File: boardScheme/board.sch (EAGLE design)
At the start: 24 parts, among them IC1 MEGA32-P, Q1 BC547, Q10 BC547, Q11 BC547, Q12 BC547, Q13 BC547, Q14 BC547, Q2 BC547, Q3 BC547, Q4 BC547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

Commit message: Changed board scheme.
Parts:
- added R1, R10, R11, R12, R13, R14, R2, R3, R4, R5, R6, R7, R8, R9: 10K, eagle-ltspice:R0204/7
- added R15, R16: 80R, eagle-ltspice:R0204/7
- added R17, R18, R19, R20, R21, R22, R23, R24: (no value), eagle-ltspice:R0204/7
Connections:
- new net N$23: Q2.B
- new net N$25: Q1.B, R1.2
- new net N$30: IC1.(AIN0/INT2)PB2, R3.1
- new net N$31: IC1.(AIN1/OC0)PB3, R4.1
- new net N$32: IC1.(SS)PB4, R5.1
- new net N$33: IC1.(MOSI)PB5, R6.1
- new net N$49: IC1.(MISO)PB6, R7.1
- new net N$50: IC1.(SCK)PB7, R8.1
- new net N$51: Q14.B, R9.2
- new net N$53: Q9.B, R11.2
- new net N$54: Q11.B, R13.2
- new net N$55: Q10.B, R12.2
- new net N$56: Q12.B, R14.2
- new net N$57: LED4.A, R15.2
- new net N$58: LED5.A, R16.2
- new net N$59: Q1.E, R17.2
- new net N$60: Q2.E, R18.2
- new net N$61: Q3.E, R19.2
- new net N$62: Q4.E, R20.2
- new net N$63: Q5.E, R21.2
- new net N$64: Q6.E, R22.2
- new net N$65: Q7.E, R23.2
- new net N$66: Q8.E, R24.2
- net N$11: now also R1.1; no longer Q1.B
- net N$13: now also R2.2
- net N$14: now also R2.1; no longer Q2.B
- net N$15: now also R3.2; no longer IC1.(AIN0/INT2)PB2
- net N$16: now also R4.2; no longer IC1.(AIN1/OC0)PB3
- net N$17: now also R5.2; no longer IC1.(SS)PB4
- net N$18: now also R6.2; no longer IC1.(MOSI)PB5
- net N$19: now also R7.2; no longer IC1.(MISO)PB6
- net N$20: now also R8.2; no longer IC1.(SCK)PB7
- net N$21: now also R17.1; no longer Q1.E
- net N$22: now also R20.1; no longer Q4.E
- net N$24: now also R18.1; no longer Q2.E
- net N$26: now also R19.1; no longer Q3.E
- net N$27: now also R23.1; no longer Q7.E
- net N$28: now also R21.1; no longer Q5.E
- net N$29: now also R11.1; no longer Q9.B
- net N$3: now also Q13.B, R10.2; no longer IC1.(OC1B)PD4, Q14.B
- net N$34: now also R12.1; no longer Q10.B
- net N$35: now also R24.1; no longer Q8.E
- net N$40: now also R13.1; no longer Q11.B
- net N$41: now also R14.1; no longer Q12.B
- net N$42: now also IC1.(OC2)PD7, R10.1, R9.1; no longer IC1.(OC1A)PD5, Q13.B
- net N$43: now also R15.1; no longer LED4.A
- net N$45: now also R16.1; no longer LED5.A
- net N$48: now also R22.1; no longer Q6.E
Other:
- moved on the sheet: LED4, LED5

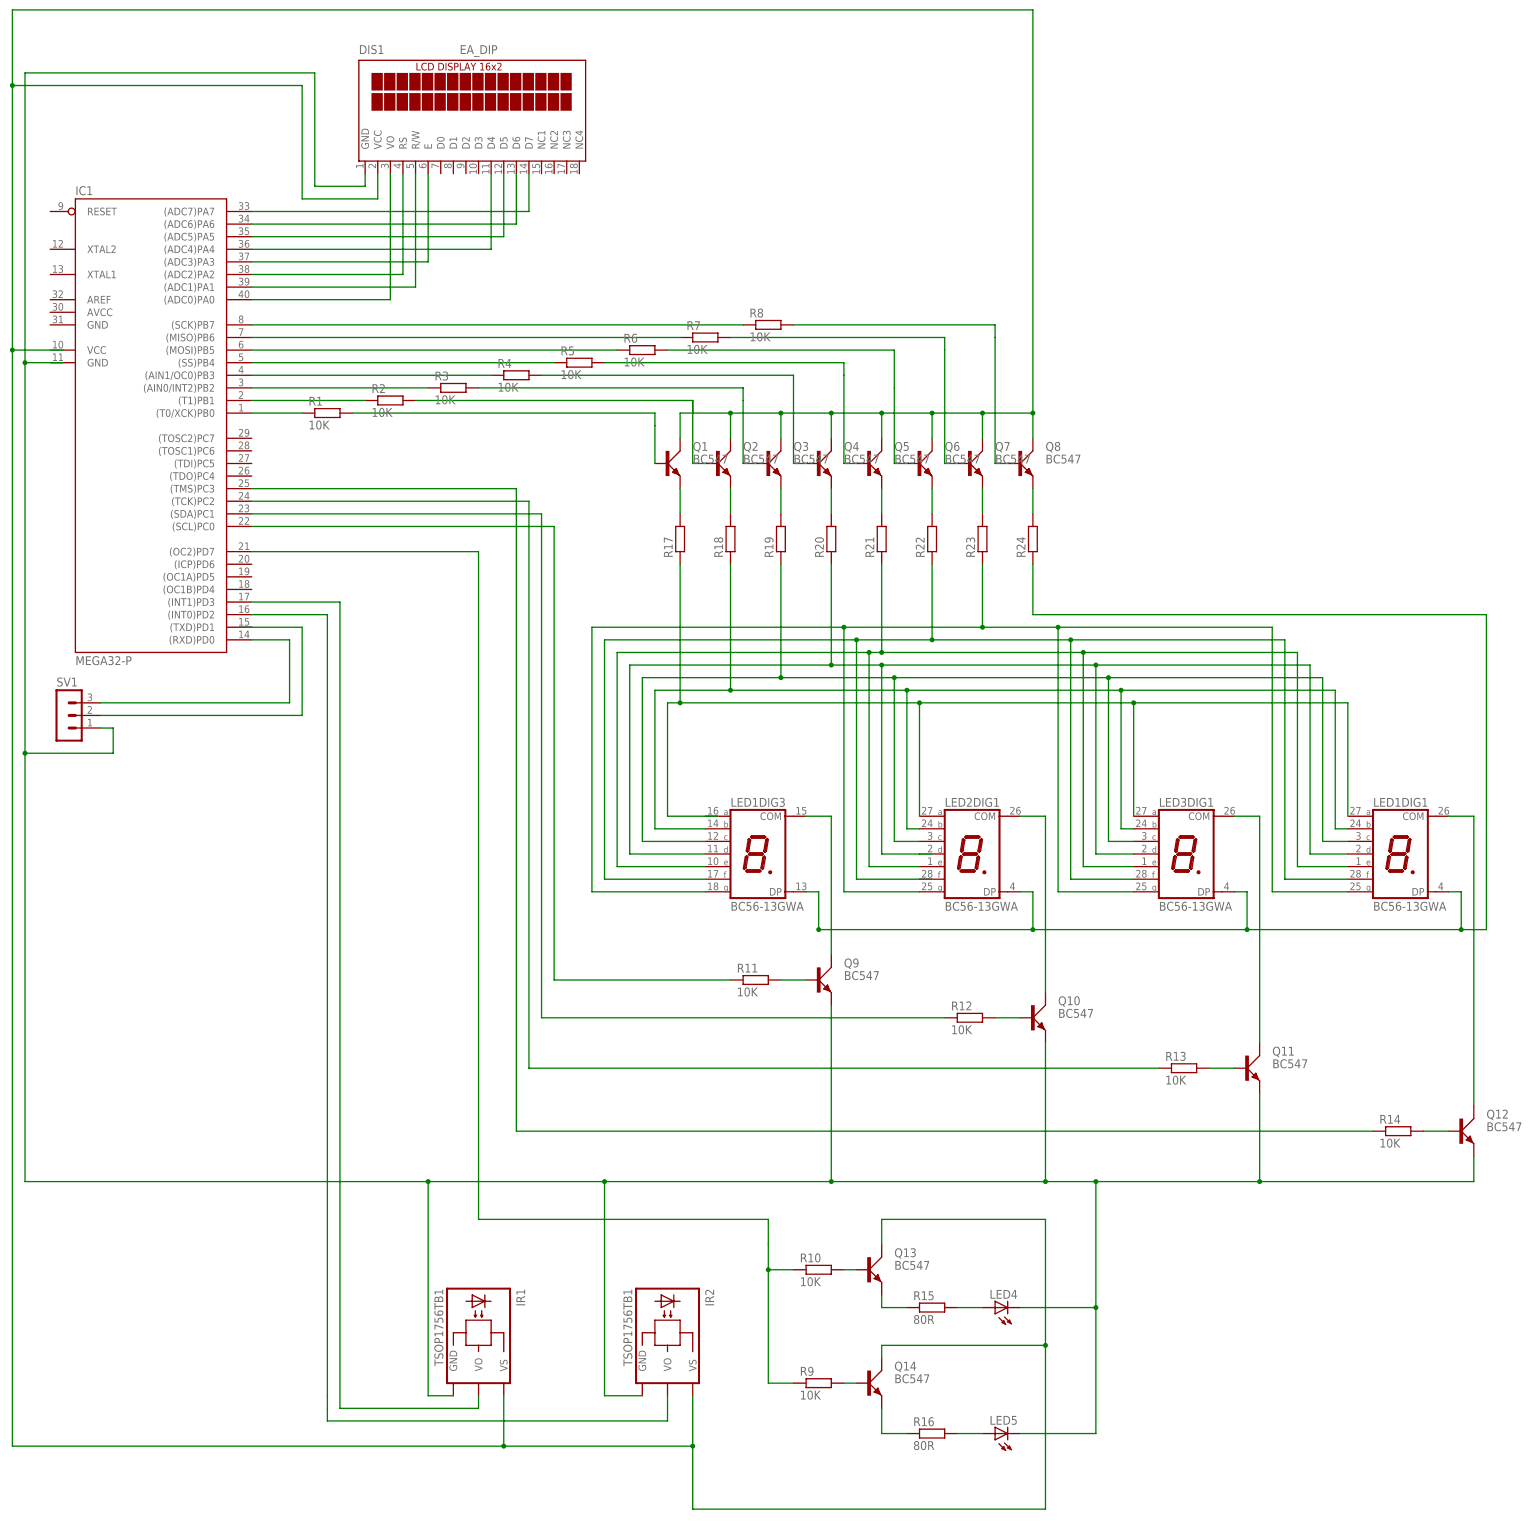
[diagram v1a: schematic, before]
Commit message: Changed board scheme. Added switches and extra transistors for steering LEDs.
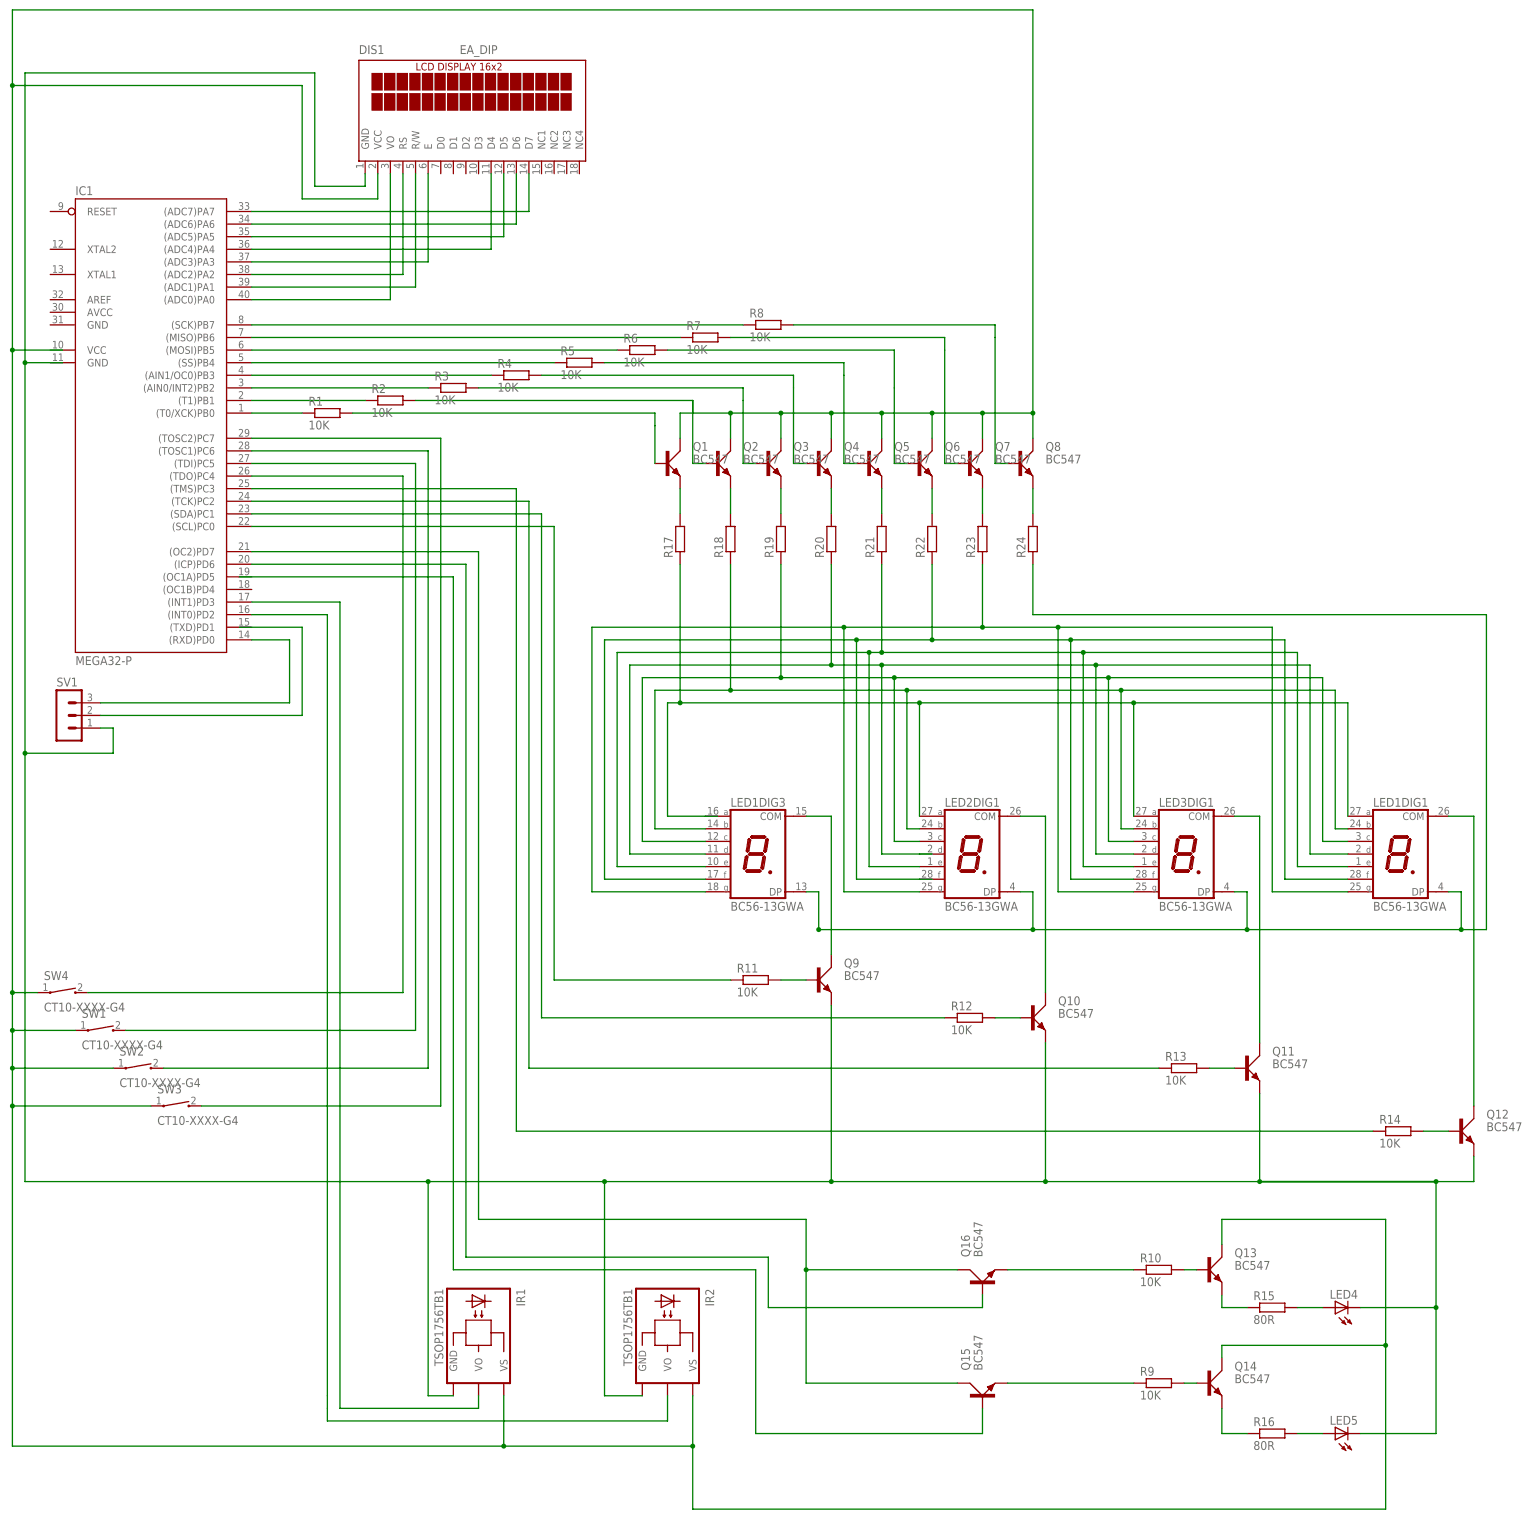
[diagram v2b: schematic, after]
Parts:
- added Q15, Q16: BC547, transistor-small-signal:BC547
- added SW1, SW2, SW3, SW4: CT10-XXXX-G4, switch-coto:CT10-XXXX-G4
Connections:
- new net N$52: Q16.E, R10.1
- new net N$67: Q15.E, R9.1
- new net N$68: IC1.(ICP)PD6, Q16.B
- new net N$69: Q15.B
- new net N$70: IC1.(TOSC2)PC7, SW3.2
- new net N$71: IC1.(TOSC1)PC6, SW2.2
- new net N$72: IC1.(TDI)PC5, SW1.2
- new net N$73: IC1.(TDO)PC4, SW4.2
- net N$13: now also SW1.1, SW2.1, SW3.1, SW4.1
- net N$42: now also Q15.C, Q16.C; no longer R10.1, R9.1
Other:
- moved on the sheet: LED4, LED5, Q13, Q14, R10, R15, R16, R9

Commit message: Changed board scheme.
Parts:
- removed Q15: BC547, transistor-small-signal:BC547
- removed R9: 10K, eagle-ltspice:R0204/7
- added Q17: BC547, transistor-small-signal:BC547
- added R25, R26, R27: 10K, eagle-ltspice:R0204/7
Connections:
- removed net N$52 (its old number): Q16.E, R10.1
- new net N$3: Q16.B, R25.2
- new net N$75: Q16.C, R15.1
- new net N$76: Q13.C, Q16.E
- net N$13: now also LED4.A, LED5.C; no longer Q13.C, Q14.C, SW1.1, SW2.1, SW3.1, SW4.1
- net N$42: now also R25.1, R26.1; no longer Q15.C, Q16.C
- net N$43: now also Q14.B, R26.2; no longer Q13.E, R15.1
- net N$44: now also Q13.E, Q17.E, SW1.1, SW2.1, SW3.1, SW4.1; no longer LED4.C, LED5.C
- net N$45: now also Q14.C; no longer Q14.E
- net N$51: now also Q14.E, Q17.C; no longer Q14.B, R9.2
- net N$57: now also LED4.C; no longer LED4.A
- net N$67: now also Q17.B, R27.2; no longer Q15.E, R9.1
- net N$68: now also R10.1; no longer Q16.B
- net N$69: now also R27.1; no longer Q15.B
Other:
- moved on the sheet: IR1, IR2, LED4, LED5, Q13, Q14, Q16, R10, R15, R16

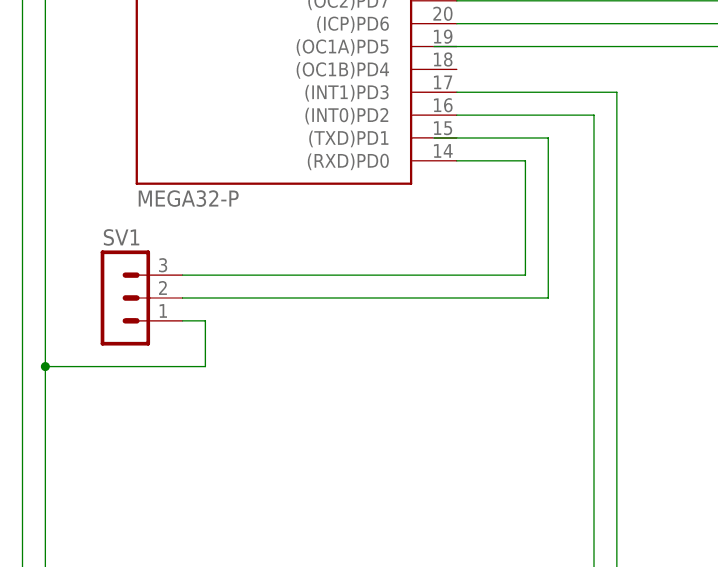
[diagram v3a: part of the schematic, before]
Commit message: Adding comments to the menu and keyboard files.
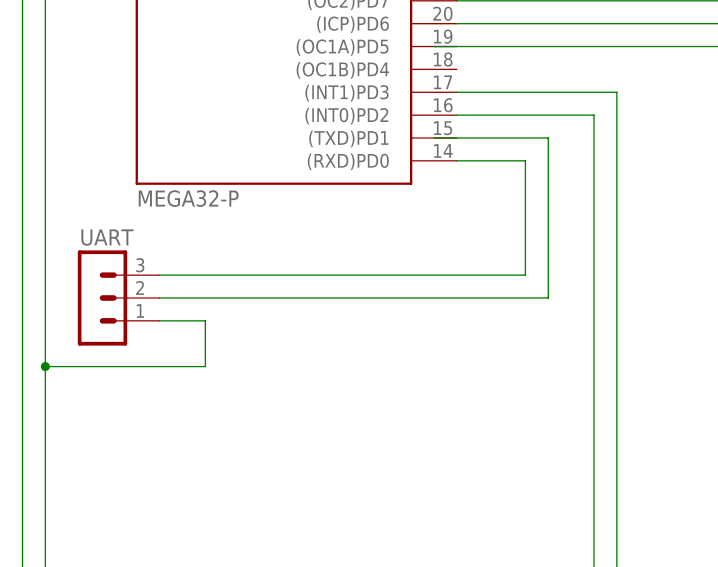
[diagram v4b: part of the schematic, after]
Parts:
- removed SV1: (no value), con-lstb:MA03-1
- added UART: (no value), con-lstb:MA03-1
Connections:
- net N$1: now also UART.2; no longer SV1.2
- net N$2: now also UART.3; no longer SV1.3
- net N$44: now also UART.1; no longer SV1.1
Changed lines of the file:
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@@
 <part name="LED4" library="eagle-ltspice" deviceset="LED_E" device=""/>
 <part name="LED5" library="eagle-ltspice" deviceset="LED_E" device=""/>
-<part name="SV1" library="con-lstb" deviceset="MA03-1" device=""/>
+<part name="UART" library="con-lstb" deviceset="MA03-1" device=""/>
 <part name="R1" library="eagle-ltspice" deviceset="R" device="0204/7" value="10K"/>
 <part name="R2" library="eagle-ltspice" deviceset="R" device="0204/7" value="10K"/>
@@
 <instance part="LED4" gate="G$1" x="228.6" y="-101.6" rot="R270"/>
 <instance part="LED5" gate="G$1" x="228.6" y="-132.08" rot="R270"/>
-<instance part="SV1" gate="G$1" x="-48.26" y="17.78"/>
+<instance part="UART" gate="G$1" x="-50.8" y="17.78"/>
 <instance part="R1" gate="G$1" x="5.08" y="78.74"/>
 <instance part="R2" gate="G$1" x="17.78" y="81.28"/>
@@
 <wire x1="-12.7" y1="35.56" x2="0" y2="35.56" width="0.1524" layer="91"/>
 <wire x1="0" y1="35.56" x2="0" y2="17.78" width="0.1524" layer="91"/>
-<wire x1="0" y1="17.78" x2="-40.64" y2="17.78" width="0.1524" layer="91"/>
-<pinref part="SV1" gate="G$1" pin="2"/>
+<wire x1="0" y1="17.78" x2="-43.18" y2="17.78" width="0.1524" layer="91"/>
+<pinref part="UART" gate="G$1" pin="2"/>
 </segment>
 </net>
@@
 <wire x1="-10.16" y1="33.02" x2="-2.54" y2="33.02" width="0.1524" layer="91"/>
 <wire x1="-2.54" y1="33.02" x2="-2.54" y2="20.32" width="0.1524" layer="91"/>
-<wire x1="-2.54" y1="20.32" x2="-40.64" y2="20.32" width="0.1524" layer="91"/>
-<pinref part="SV1" gate="G$1" pin="3"/>
+<wire x1="-2.54" y1="20.32" x2="-43.18" y2="20.32" width="0.1524" layer="91"/>
+<pinref part="UART" gate="G$1" pin="3"/>
 </segment>
 </net>
@@
 <junction x="-55.88" y="88.9"/>
 <wire x1="-55.88" y1="88.9" x2="-55.88" y2="10.16" width="0.1524" layer="91"/>
-<pinref part="SV1" gate="G$1" pin="1"/>
-<wire x1="-40.64" y1="15.24" x2="-38.1" y2="15.24" width="0.1524" layer="91"/>
+<pinref part="UART" gate="G$1" pin="1"/>
+<wire x1="-43.18" y1="15.24" x2="-38.1" y2="15.24" width="0.1524" layer="91"/>
 <wire x1="-38.1" y1="15.24" x2="-38.1" y2="10.16" width="0.1524" layer="91"/>
 <wire x1="-38.1" y1="10.16" x2="-55.88" y2="10.16" width="0.1524" layer="91"/>
